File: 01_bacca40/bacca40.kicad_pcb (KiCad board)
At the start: 2 copper layers, 245.3 x 76.5 mm, 110 parts, among them J1 TYPE-C-31-M12_13, J2 AVR-ISP-6_mod, K1 KEYSW, K10 KEYSW, K11 KEYSW, K12 KEYSW, K13 KEYSW, K14 KEYSW, K15 KEYSW, K16 KEYSW, K17 KEYSW, K18 KEYSW, K19 KEYSW, K2 KEYSW, K20 KEYSW, K21 KEYSW, K22 KEYSW, K23 KEYSW, K24 KEYSW, K25 KEYSW, K26 KEYSW, K27 KEYSW, K28 KEYSW, K29 KEYSW, K3 KEYSW, K30 KEYSW, K31 KEYSW, K32 KEYSW, K33 KEYSW, K34 KEYSW, K35 KEYSW, K36 KEYSW, K37 KEYSW, K38 KEYSW, K39 KEYSW, K4 KEYSW, K40 KEYSW, K41 KEYSW, K42 KEYSW, K5 KEYSW, K6 KEYSW, K7 KEYSW, K8 KEYSW, K9 KEYSW, SW1 SW_PUSH, U1 ATMEGA32U4, U3 USBLC6-2SC6, Y1 16MHz

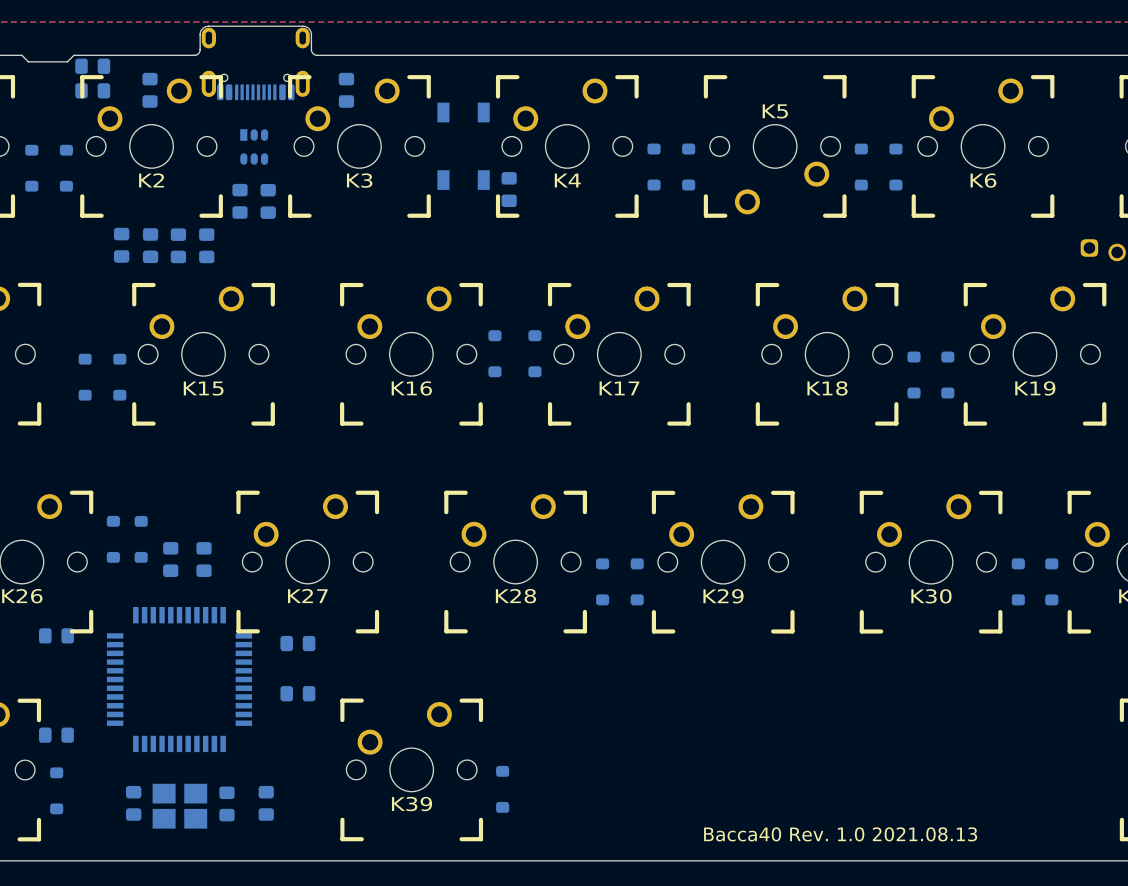
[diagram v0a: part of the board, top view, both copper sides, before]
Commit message: USB/MCU routed
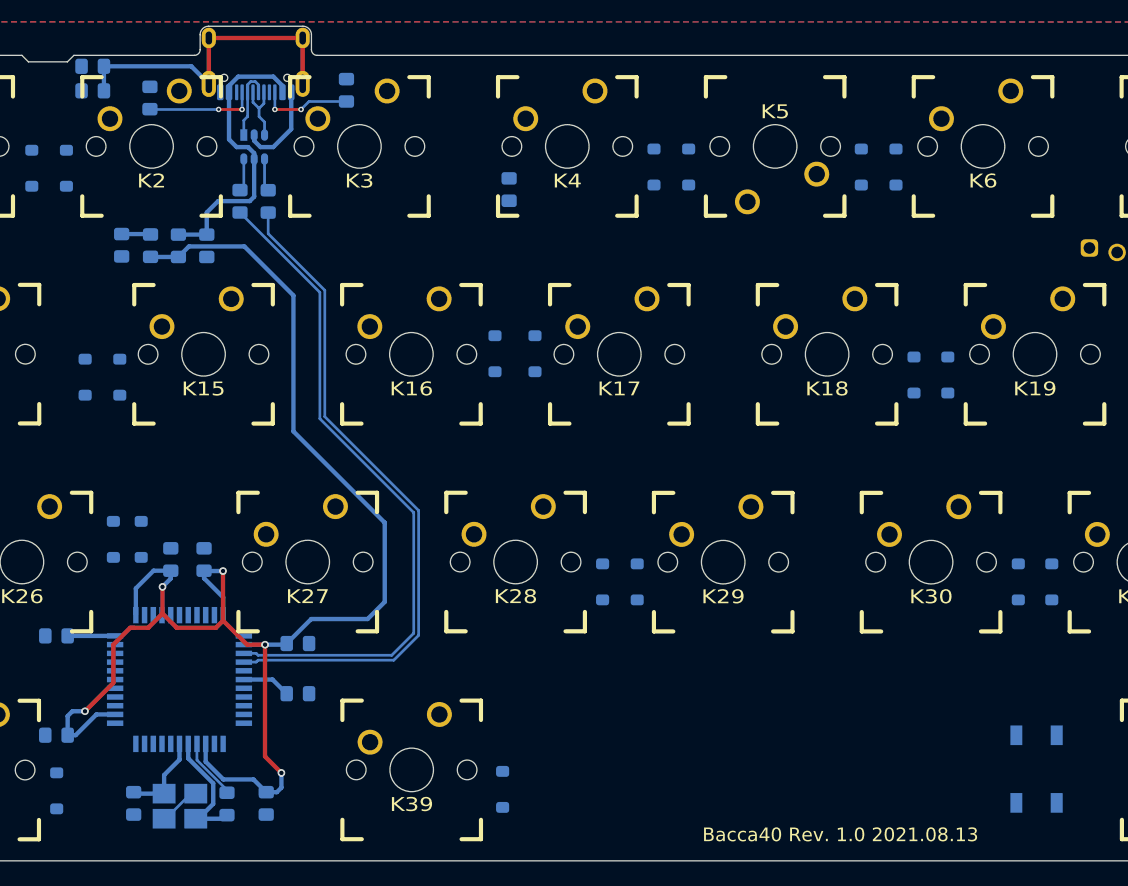
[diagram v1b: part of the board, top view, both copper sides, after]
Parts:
- moved SW1 77.5 mm to (187.0, 110.3)
- moved RCC1 0.71 mm to (105.8, 48.8)
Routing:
- net VCC: track 0.00 -> 139.4 mm, vias 0 -> 5
- net D-: track 0.00 -> 61.6 mm
- net D+: track 0.00 -> 61.5 mm
- net Net-(C7-Pad1): track 0.00 -> 29.5 mm
- net VBUS: track 0.00 -> 26.9 mm
- net GND: track 0.00 -> 18.2 mm
- net XTAL1: track 0.00 -> 11.6 mm
- net Net-(J1-PadA5): track 0.00 -> 10.6 mm, vias 0 -> 2
- net Net-(J1-PadB5): track 0.00 -> 8.99 mm, vias 0 -> 2
- net XTAL2: track 0.00 -> 7.99 mm
- net DBUS+: track 0.00 -> 7.11 mm
- net DBUS-: track 0.00 -> 6.13 mm
- net Net-(C6-Pad1): track 0.00 -> 4.46 mm
- net Net-(R1-Pad2): track 0.00 -> 4.35 mm
- net Net-(R3-Pad2): track 0.00 -> 3.00 mm
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
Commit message: Fully routed?
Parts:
- K40: footprint Keebio-Parts:MX_Plate_625H -> Keebio-Parts:MX_PCB_625H
- RSW1, SW1: moved to F.Cu
- moved RSW1 73.9 mm to (192.1, 108.2), turned to 270 degrees
- moved J2 73.0 mm to (141.5, 108.6), turned to 0 degrees
- moved CESD1 19.8 mm to (91.2, 60.6)
- moved F1 19.8 mm to (88.7, 60.6)
- moved LED1 19.8 mm to (83.5, 60.6)
- moved R4 19.8 mm to (86.1, 60.6)
- moved D41 19.6 mm to (281.5, 112.3)
- moved D4 19.1 mm to (136.1, 55.1)
- moved D3 19.1 mm to (132.9, 55.1)
- moved R2 19.0 mm to (95.0, 58.2)
- moved J1 19.0 mm to (96.4, 49.0)
- moved R3 19.0 mm to (97.6, 58.2)
- moved U3 19.0 mm to (96.3, 53.2)
- moved D1 18.9 mm to (113.9, 55.2)
- moved D2 18.9 mm to (117.0, 55.2)
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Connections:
- net enc0b renamed Net-(U1-Pad20)
- K1 pad 1: col1 -> col0
- K10 pad 1: col10 -> col9
- K11 pad 1: col11 -> col10
- K12 pad 1: col0 -> col11
- K14 pad 1: col1 -> col0
- K15 pad 1: col2 -> col1
- K16 pad 1: col3 -> col2
- K17 pad 1: col4 -> col3
- K18 pad 1: col5 -> col4
- K19 pad 1: col6 -> col5
- K2 pad 1: col2 -> col1
- K20 pad 1: col7 -> col6
- K21 pad 1: col8 -> col7
- K22 pad 1: col9 -> col8
- K23 pad 1: col10 -> col9
- K24 pad 1: col11 -> col10
- K25 pad 1: col0 -> col11
- K26 pad 1: col1 -> col0
- K27 pad 1: col2 -> col1
- K28 pad 1: col3 -> col2
- K29 pad 1: col4 -> col3
- K3 pad 1: col3 -> col2
- K30 pad 1: col5 -> col4
- K31 pad 1: col6 -> col5
- K32 pad 1: col7 -> col6
- K33 pad 1: col8 -> col7
- K34 pad 1: col9 -> col8
- K35 pad 1: col10 -> col9
- K36 pad 1: col11 -> col10
- K37 pad 1: col0 -> col11
- K38 pad 1: col1 -> col0
- K39 pad 1: col3 -> col2
- K4 pad 1: col4 -> col3
- K40 pad 1: col6 -> col5
- K41 pad 1: col10 -> col9
- K42 pad 1: col0 -> col11
- K5 pad 1: col5 -> col4
- K6 pad 1: col6 -> col5
- K7 pad 1: col7 -> col6
- K8 pad 1: col8 -> col7
- K9 pad 1: col9 -> col8
- U1 pad 1: col8 -> col7
- U1 pad 10: col11 -> col10
- U1 pad 11: col0 -> col11
- U1 pad 12: col3 -> col2
- U1 pad 21: enc0a -> col12
- U1 pad 22: col2 -> Net-(U1-Pad22)
- U1 pad 25: row2 -> row3
- U1 pad 26: row3 -> col0
- U1 pad 27: col1 -> Net-(U1-Pad27)
- U1 pad 31: col12 -> col1
- U1 pad 32: Net-(U1-Pad32) -> row2
- U1 pad 38: col4 -> col3
- U1 pad 39: col5 -> col4
- U1 pad 40: col6 -> col5
- U1 pad 41: col7 -> col6
- U1 pad 8: col9 -> col8
- U1 pad 9: col10 -> col9
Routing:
- net col11: track 0.00 -> 276.1 mm, vias 0 -> 3
- net col12: track 0.00 -> 266.2 mm, vias 0 -> 2
- net col10: track 0.00 -> 266.0 mm, vias 0 -> 3
- net row0: track 0.00 -> 241.7 mm, vias 0 -> 4
- net row2: track 0.00 -> 231.1 mm, vias 0 -> 4
- net row3: track 0.00 -> 227.3 mm
- net col9: track 0.00 -> 220.2 mm, vias 0 -> 1
- net row1: track 0.00 -> 218.9 mm, vias 0 -> 4
- net col8: track 0.00 -> 190.6 mm, vias 0 -> 1
- net col6: track 0.00 -> 185.8 mm, vias 0 -> 3
- net col5: track 0.00 -> 169.0 mm, vias 0 -> 3
- net col7: track 0.00 -> 169.0 mm, vias 0 -> 3
- net col0: track 0.00 -> 139.8 mm, vias 0 -> 2
- net col4: track 0.00 -> 137.5 mm, vias 0 -> 3
- net col3: track 0.00 -> 119.9 mm, vias 0 -> 3
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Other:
- board size 245.3 x 76.5 mm -> 245.3 x 78.9 mm
